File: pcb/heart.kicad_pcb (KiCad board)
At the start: 2 copper layers, 119.1 x 105.8 mm, 43 parts

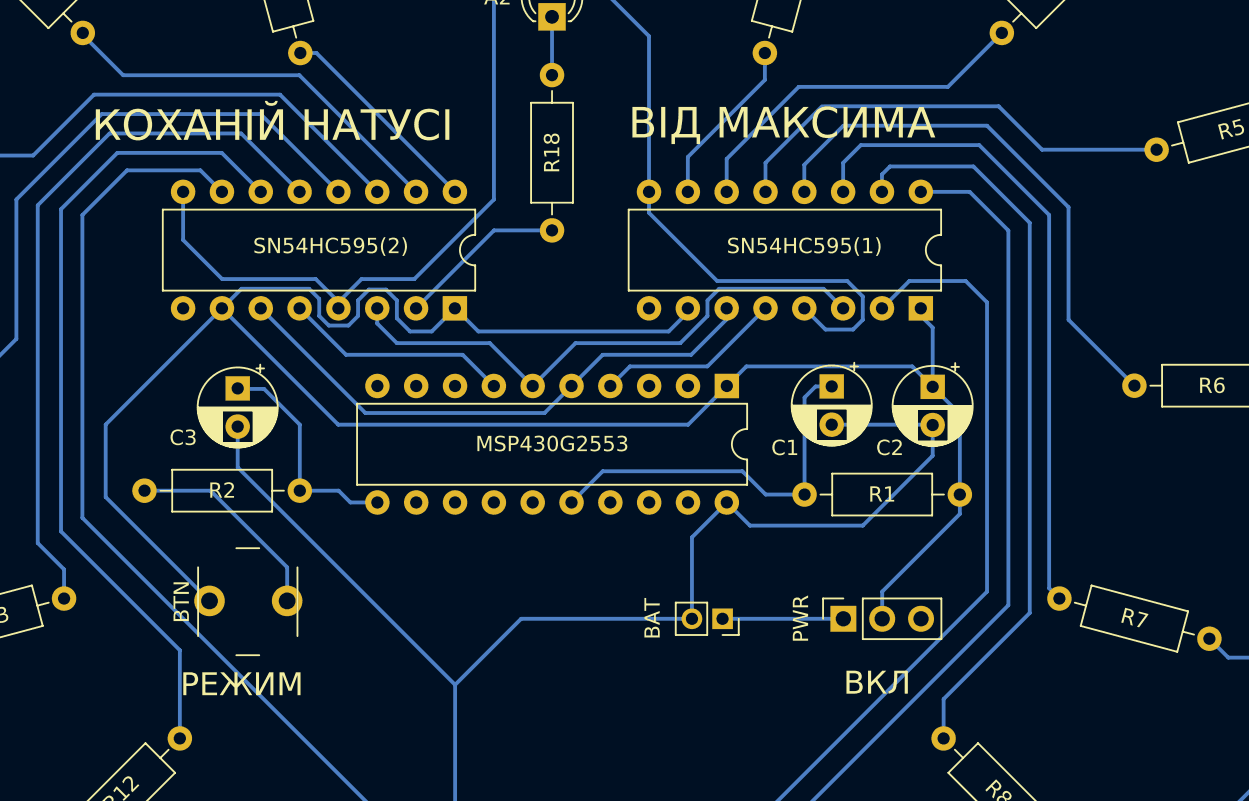
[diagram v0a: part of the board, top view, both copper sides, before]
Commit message: Remove name from silkscreen
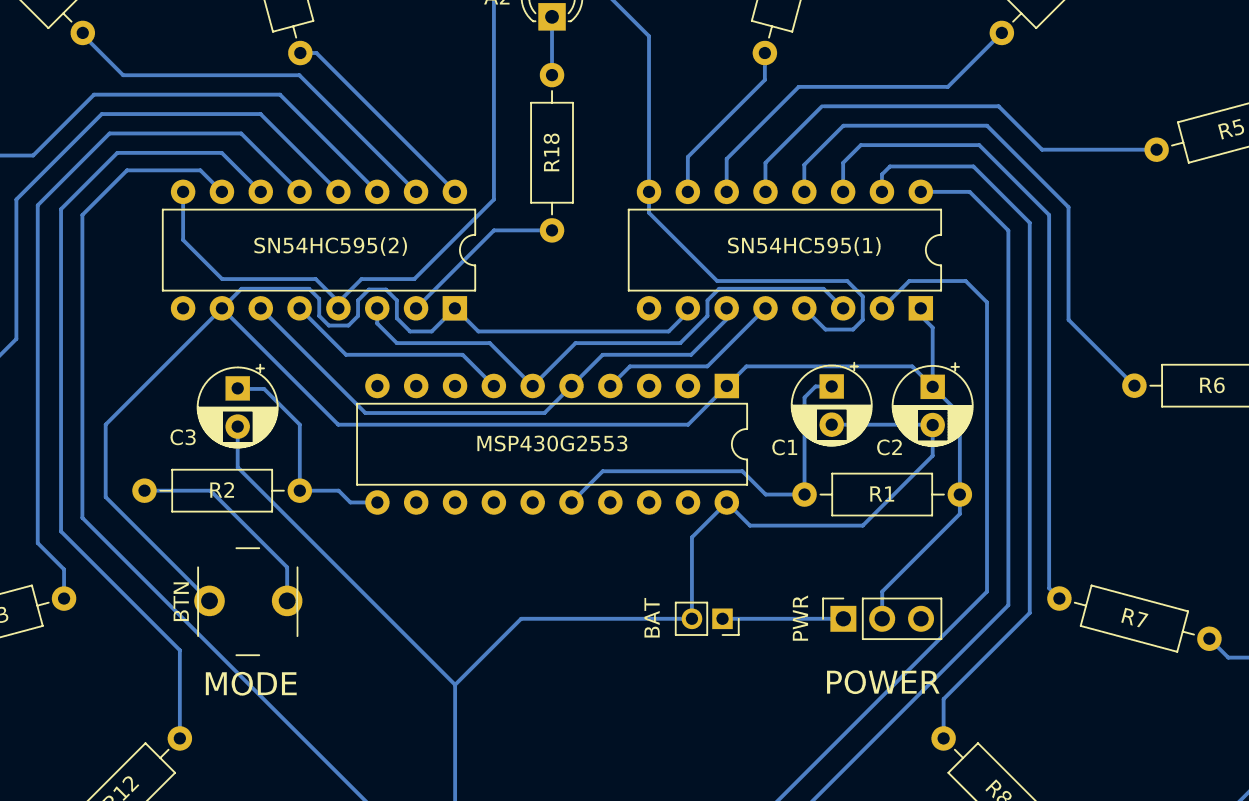
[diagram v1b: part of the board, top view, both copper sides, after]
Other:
- board text added: "MODE"
- board text added: "POWER"
- board text removed: "ВІД МАКСИМА"
- board text removed: "ВКЛ"
- board text removed: "КОХАНІЙ НАТУСІ"
- board text removed: "РЕЖИМ"
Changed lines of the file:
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@@
     (pcbplotparams
       (layerselection 0x00010fc_ffffffff)
-      (plot_on_all_layers_selection 0x0000000_00000000)
+      (plot_on_all_layers_selection 0x0001010_80000000)
       (disableapertmacros false)
       (usegerberextensions false)
@@
       (sketchpadsonfab false)
       (subtractmaskfromsilk false)
-      (outputformat 1)
+      (outputformat 5)
       (mirror false)
       (drillshape 0)
       (scaleselection 1)
-      (outputdirectory "")
+      (outputdirectory "../media/")
     )
   )
@@
     )
     (stroke (width 0.1) (type solid)) (fill none) (layer "Edge.Cuts"))
-  (gr_text "КОХАНІЙ НАТУСІ" (at 118.4656 74.3204) (layer "F.SilkS")
-    (effects (font (size 2 2) (thickness 0.3)) (justify left bottom))
-  )
-  (gr_text "ВІД МАКСИМА" (at 153.5684 74.168) (layer "F.SilkS")
-    (effects (font (size 2 2) (thickness 0.3)) (justify left bottom))
-  )
-  (gr_text "ВКЛ" (at 167.64 110.49) (layer "F.SilkS")
+  (gr_text "POWER" (at 166.37 110.49) (layer "F.SilkS")
     (effects (font (size 1.5 1.5) (thickness 0.3)) (justify left bottom))
   )
-  (gr_text "РЕЖИМ" (at 124.2568 110.5916) (layer "F.SilkS")
+  (gr_text "MODE" (at 125.73 110.5916) (layer "F.SilkS")
     (effects (font (size 1.5 1.5) (thickness 0.3)) (justify left bottom))
   )

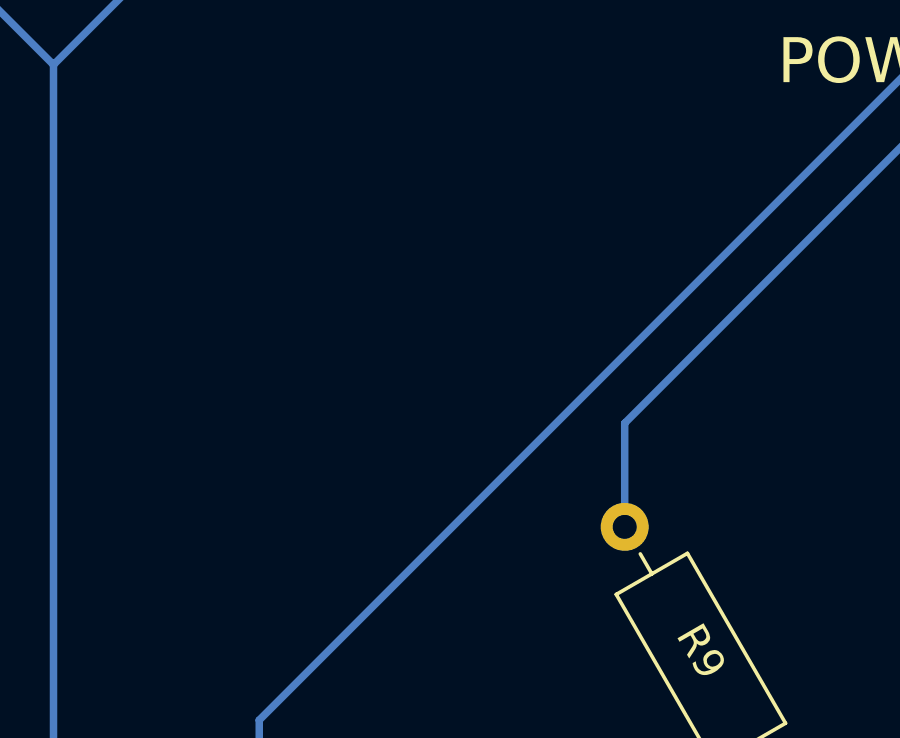
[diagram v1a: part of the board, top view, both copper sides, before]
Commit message: Add version and author to silkscreen
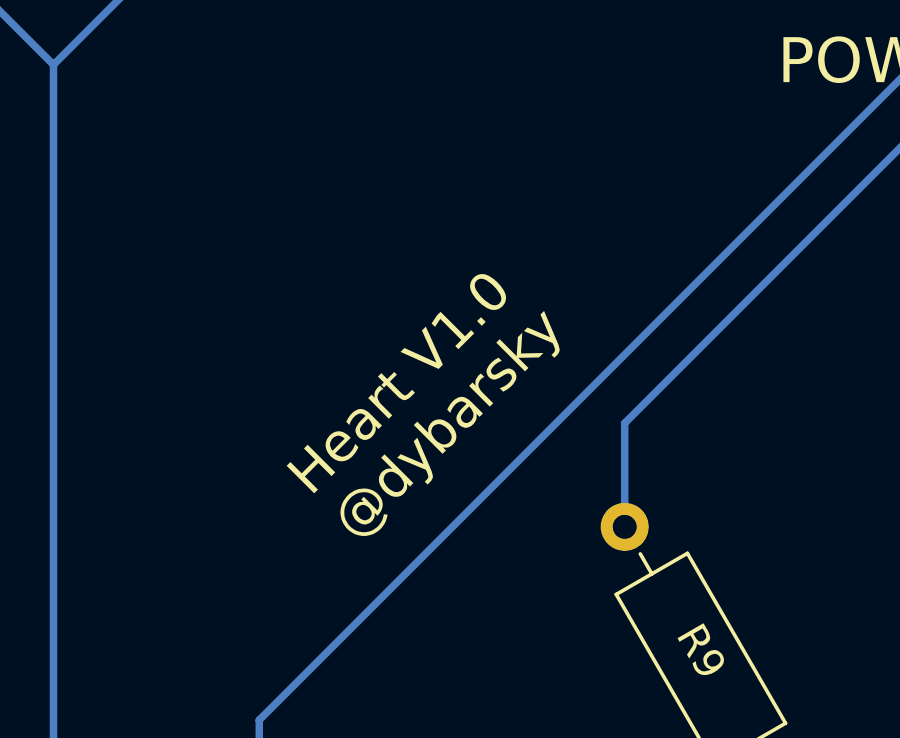
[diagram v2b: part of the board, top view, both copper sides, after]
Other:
- board text added: "Heart V1.0 @dybarsky"
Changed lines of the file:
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@@
     )
     (stroke (width 0.1) (type solid)) (fill none) (layer "Edge.Cuts"))
+  (gr_text "Heart V1.0\n@dybarsky" (at 152.4 125.73 45) (layer "F.SilkS")
+    (effects (font (size 1.3 1.3) (thickness 0.1625)) (justify left bottom))
+  )
   (gr_text "POWER" (at 166.37 110.49) (layer "F.SilkS")
     (effects (font (size 1.5 1.5) (thickness 0.3)) (justify left bottom))
